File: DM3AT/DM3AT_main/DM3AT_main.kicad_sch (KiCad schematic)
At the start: 0 parts

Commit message: Should be SD
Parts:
- added J1: DM3AT-SF-PEJM5_40_, DM3ATSFPEJM540, symbol DM3AT:DM3AT-SF-PEJM5_40_
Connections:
- new net: J1.MP1, J1.MP2, J1.MP3, J1.MP4, J1.MP5
- new net DM3AT_CD_N: J1.CD1 (CARD_DETECT)
- new net DM3AT_CS_N: J1.2 (CD/DAT3)
- new net DM3AT_MISO_N: J1.7 (DAT0)
- new net DM3AT_MOSI_0: J1.3 (CMD)
- new net DM3AT_SCLK_N: J1.5 (CLK)
- no-connect marks 0 -> 2

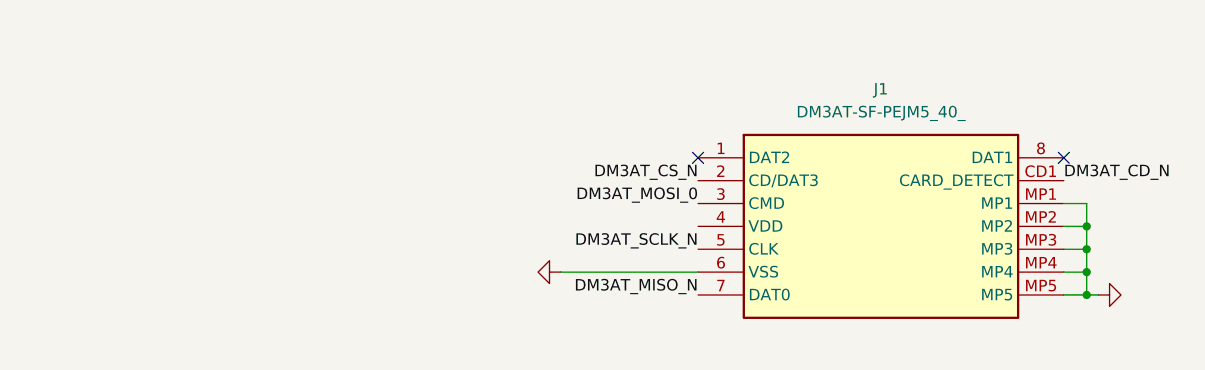
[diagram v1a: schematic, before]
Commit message: start MCU power circuit
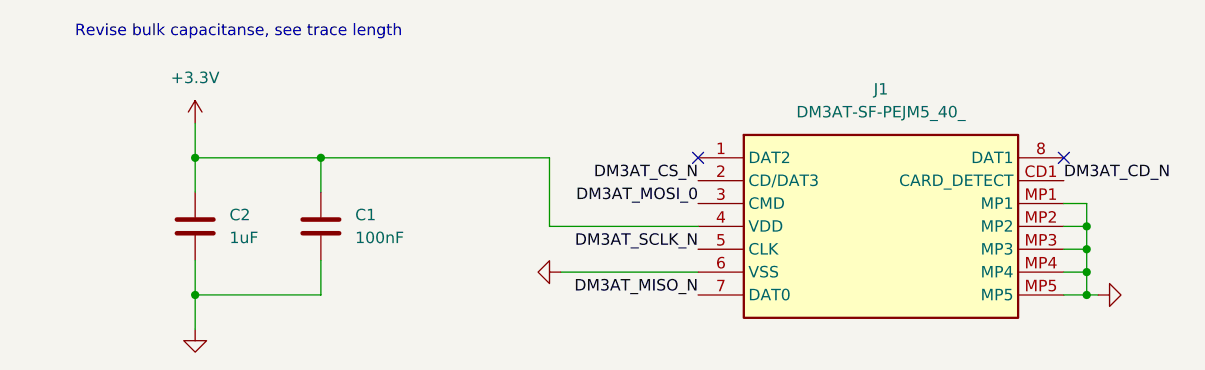
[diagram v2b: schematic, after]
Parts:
- added C1: 100nF, symbol Device:C
- added C2: 1uF, symbol Device:C
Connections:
- net +3.3V: now reaches J1.4 (VDD)
- net +3.3V: now also C1.1, C2.1
- new net: C1.2, C2.2
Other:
- note added: "Revise bulk capacitanse, see trace length"
